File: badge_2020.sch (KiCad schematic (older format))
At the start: 22 parts, among them J1 USB_A, Q1 AOI409 (LP0701N3-G), SW1 SW_Push, SW2 SW, U1 ATTINY85-20PU

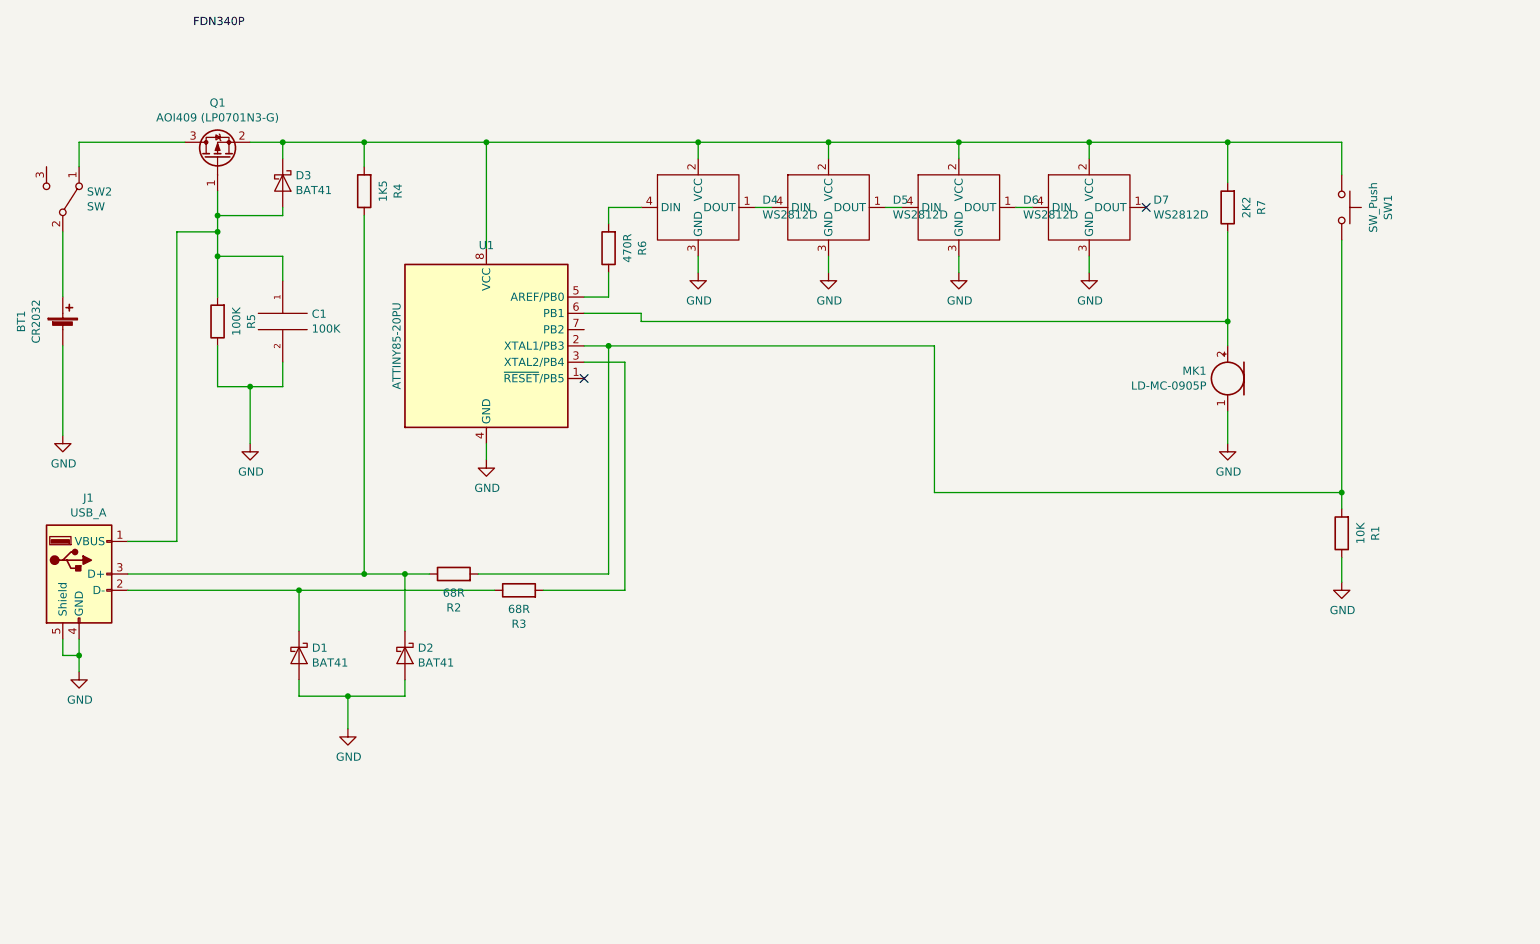
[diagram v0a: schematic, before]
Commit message: revisado y actualizado
Esta versión debería funcionar. Falta el silkscreen posterior, y quizá cambiar la huella del interruptor
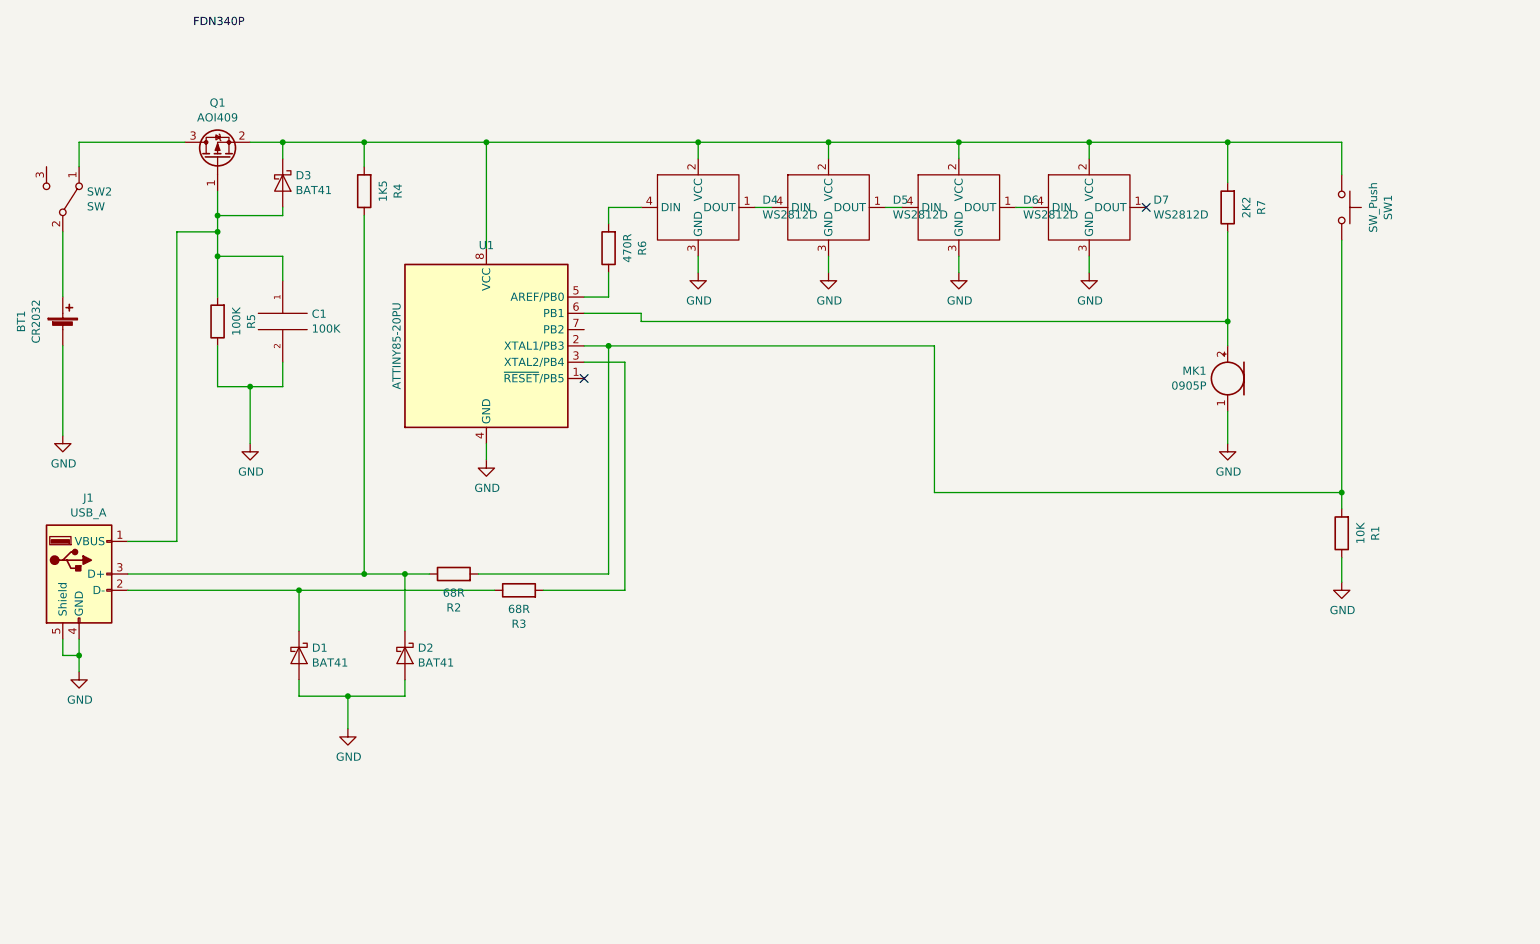
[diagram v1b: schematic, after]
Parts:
- MK1: value LD-MC-0905P -> 0905P
- Q1: value AOI409 (LP0701N3-G) -> AOI409
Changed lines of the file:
@@
 P 2850 1850
 F 0 "Q1" V 3192 1850 50  0000 C CNN
-F 1 "AOI409  (LP0701N3-G)" V 3101 1850 50  0000 C CNN
+F 1 "AOI409" V 3101 1850 50  0000 C CNN
 F 2 "Package_TO_SOT_THT:TO-251-3_Vertical" H 3050 1950 50  0001 C CNN
 F 3 "~" H 2850 1850 50  0001 C CNN
@@
 P 9050 3200
 F 0 "MK1" H 9180 3246 50  0000 L CNN
-F 1 "LD-MC-0905P" H 9180 3155 50  0000 L CNN
+F 1 "0905P" H 9180 3155 50  0000 L CNN
 F 2 "Sensor_Audio:Microphone_D10.0mm_P2.54mm" V 9050 3300 50  0001 C CNN
 F 3 "~" V 9050 3300 50  0001 C CNN

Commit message: Actualización
Versión corregida y actualizada
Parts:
- removed D1, D2: BAT41, Diode_THT:D_DO-34_SOD68_P7.62mm_Horizontal, symbol Device:D_Schottky
- added C2: 10uF, Capacitor_THT:CP_Radial_D5.0mm_P2.50mm, symbol Device:CP_Small
- added D2, D3: BZX55 3V6, Diode_THT:D_DO-34_SOD68_P7.62mm_Horizontal, symbol Device:D_Zener
- added D8: WS2812D, LED_THT:LED_D5.0mm-WS2812D, symbol Project_Symbol_Library:WS2812D
- added Imagen_1: IMAGEN OSHWI, project footprints:•OSHWI_footprint_silk, symbol badge_2020:NONE_symbol
- added Imagen_2: LOGO AMTEGA, project footprints:amtega_logo_2cm, symbol badge_2020:NONE_symbol
- added Imagen_3: LOGO BRICOLABS, project footprints:BricoLabs_logo_small, symbol badge_2020:NONE_symbol
- C1: footprint Resistor_THT:R_Axial_DIN0207_L6.3mm_D2.5mm_P10.16mm_Horizontal -> Capacitor_THT:C_Disc_D4.3mm_W1.9mm_P5.00mm
- R6: renamed from R7; value 2K2 -> 10K
- renumbered D3 to D1, R5 to R1, R4 to R2, R2 to R3, R3 to R4, R6 to R5, R1 to R7
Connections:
- net labels added: D, G, S
- net labels removed: FDN340P
- no-connect marks 2 -> 0
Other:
- moved on the sheet: BT1, C1, D1, D4, D5, D6, D7, J1, MK1, Q1, R1, R2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
